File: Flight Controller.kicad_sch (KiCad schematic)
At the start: 151 parts, among them IC2 AT7456E, J1 Conn_01x08_MountingPin, J2 USB_C_Receptacle_USB2.0_14P, Q2 BC817W, U1 AT32F435RGT7, U2 LMR51430, U3 BMP280, U4 NCP1117-3.3_SOT223, U5 LMR51430, U6 W25Q128JVSIQ TR, U7 ICM-42688-P, U8 NCP1117-3.3_SOT223, Y1 8M, Y2 27M

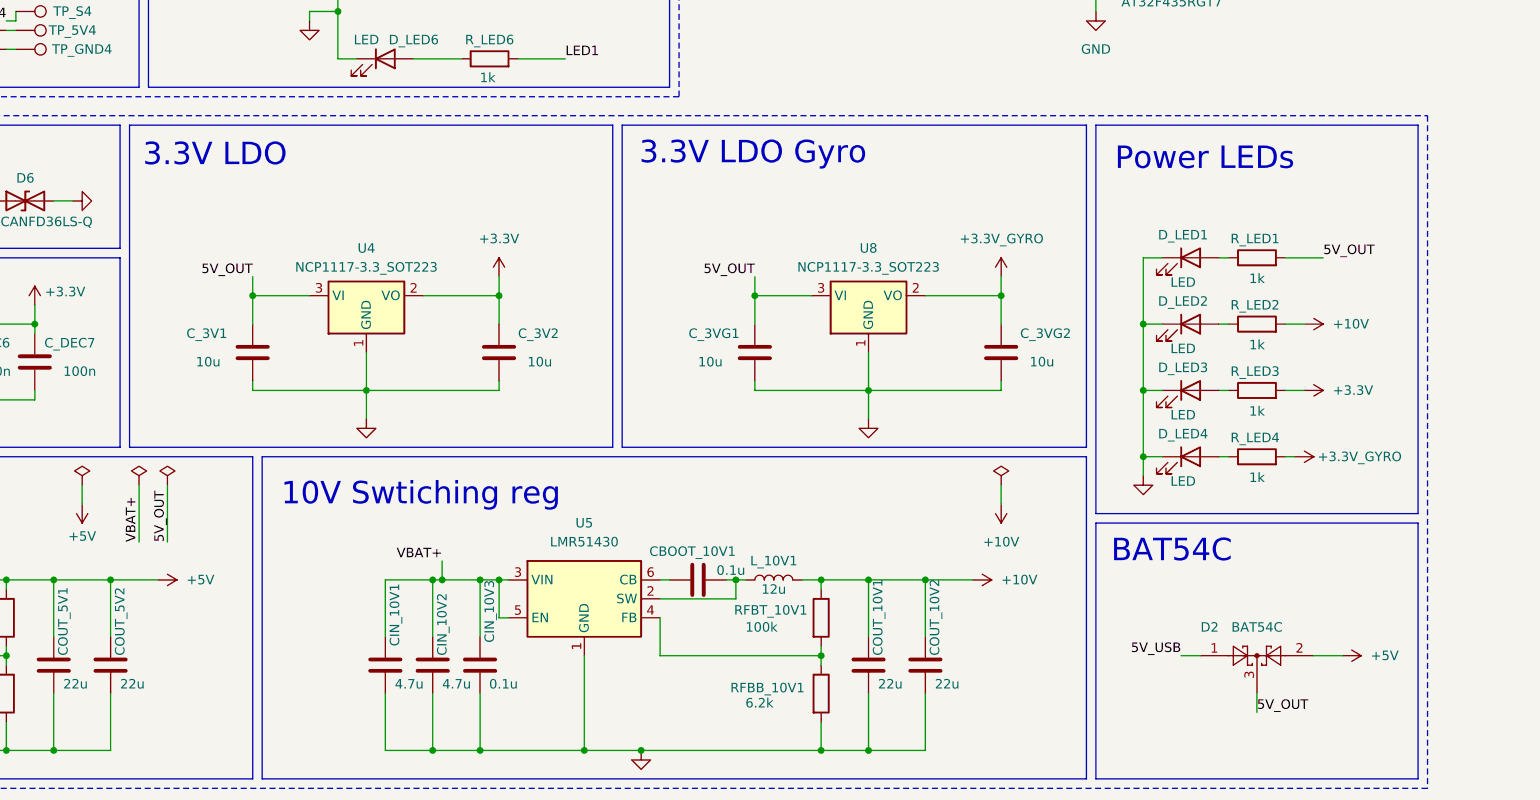
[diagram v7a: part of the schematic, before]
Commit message: Changed LDOs
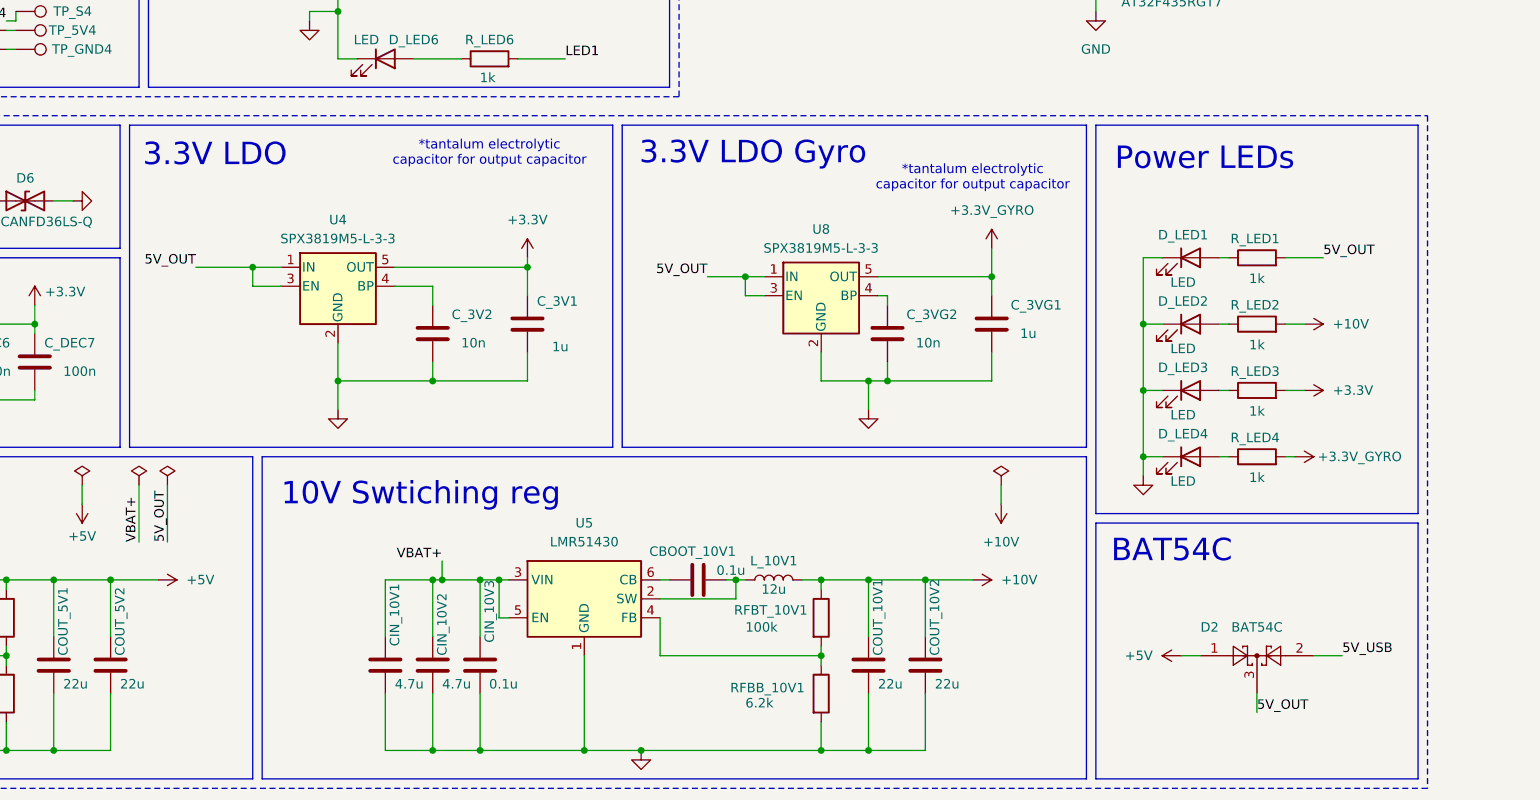
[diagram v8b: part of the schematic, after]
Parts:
- removed C_3VG1: 10u, Capacitor_SMD:C_0603_1608Metric_Pad1.08x0.95mm_HandSolder, symbol Device:C
- removed U4, U8: NCP1117-3.3_SOT223, Package_TO_SOT_SMD:SOT-223-3_TabPin2, symbol Regulator_Linear:NCP1117-3.3_SOT223
- added C_3VG2: 10n, Capacitor_SMD:C_0402_1005Metric, symbol Device:C
- added U4, U8: SPX3819M5-L-3-3, Package_TO_SOT_SMD:SOT-23-5, symbol Regulator_Linear:SPX3819M5-L-3-3
- C_3V1: value 10u -> 1u
- C_3V2: value 10u -> 10n; footprint Capacitor_SMD:C_0603_1608Metric -> Capacitor_SMD:C_0402_1005Metric
- C_3VG1: renamed from C_3VG2; value 10u -> 1u; footprint Capacitor_SMD:C_0603_1608Metric_Pad1.08x0.95mm_HandSolder -> Capacitor_SMD:C_0603_1608Metric
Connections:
- net +3.3V: now also C_3V1.1, U4.5 (OUT); no longer C_3V2.1
- net +3.3V_GYRO: now also U8.5 (OUT)
- net +5V: now also D2.1; no longer D2.2
- net 5V_OUT: now also U4.1 (IN), U4.3 (EN), U8.1 (IN), U8.3 (EN); no longer C_3V1.1
- net 5V_USB: now also D2.2; no longer D2.1
- net GND: now also C_3VG2.2, U4.2 (GND), U8.2 (GND)
- new net: C_3VG2.1, U8.4 (BP)
- new net: C_3V2.1, U4.4 (BP)
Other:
- note added: "*tantalum electrolytic capacitor for output capacitor"
- moved on the sheet: C_3V1, C_3V2, C_3VG1
